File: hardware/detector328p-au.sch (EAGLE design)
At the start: 65 parts, among them K1 SRD-05VDC-SL-C, Q1 BSS123, Q2 16MHz, T1 BC817-40SMD, T2 BC817, T3 BC817, U1 ATMEGA328P-AU

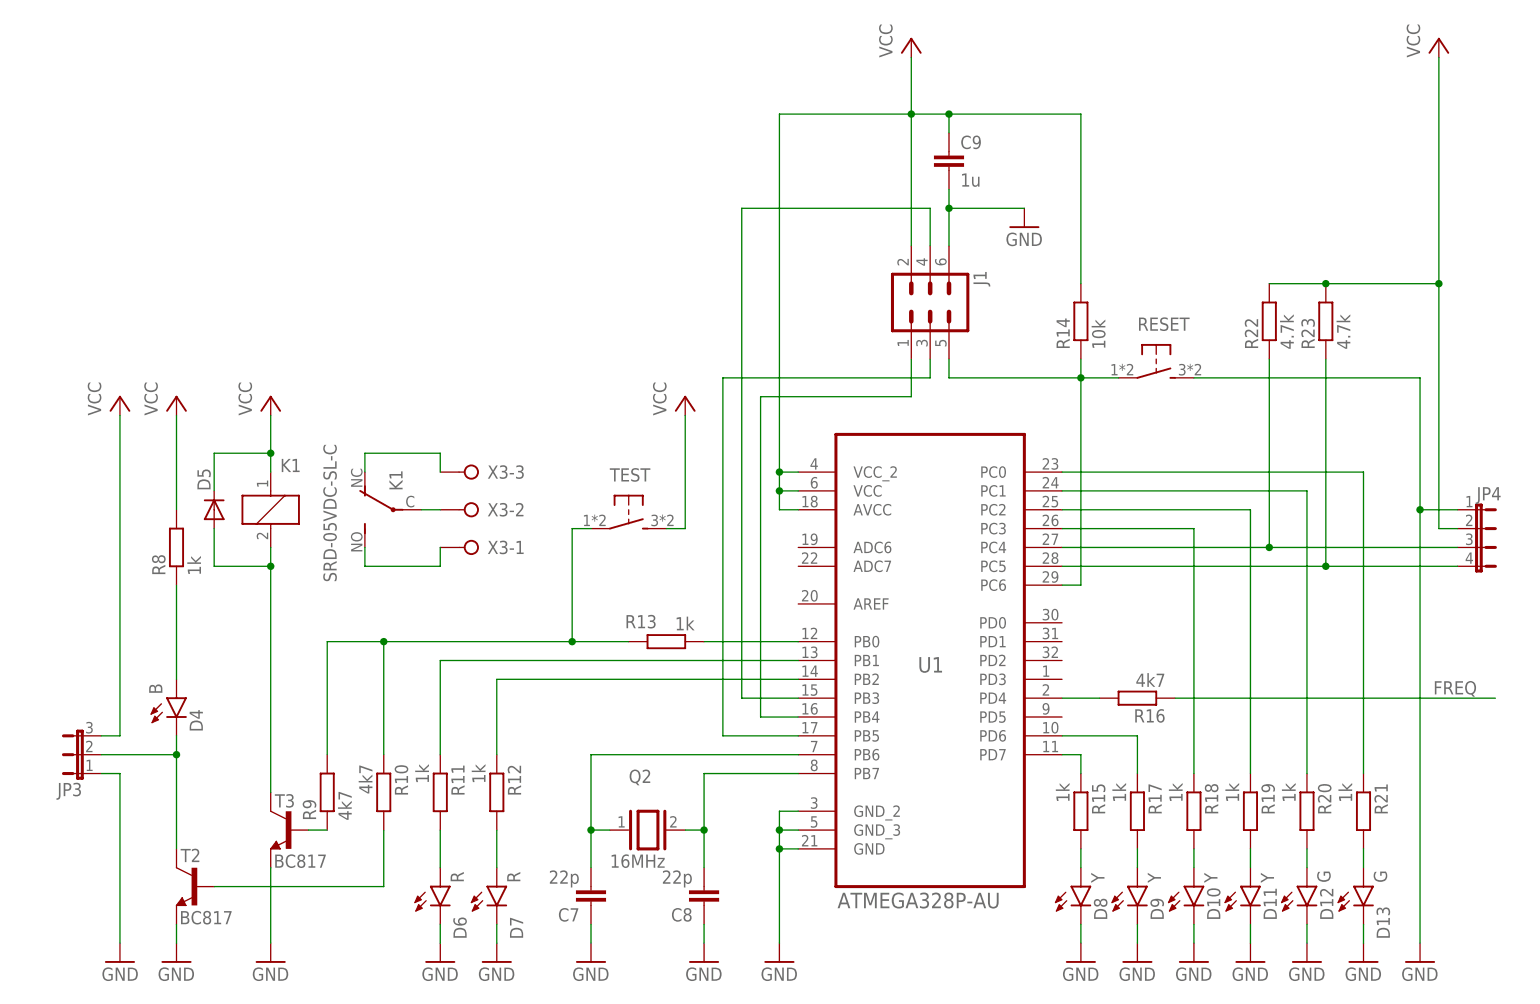
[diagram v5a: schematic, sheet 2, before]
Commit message: detector328p-au almost wired
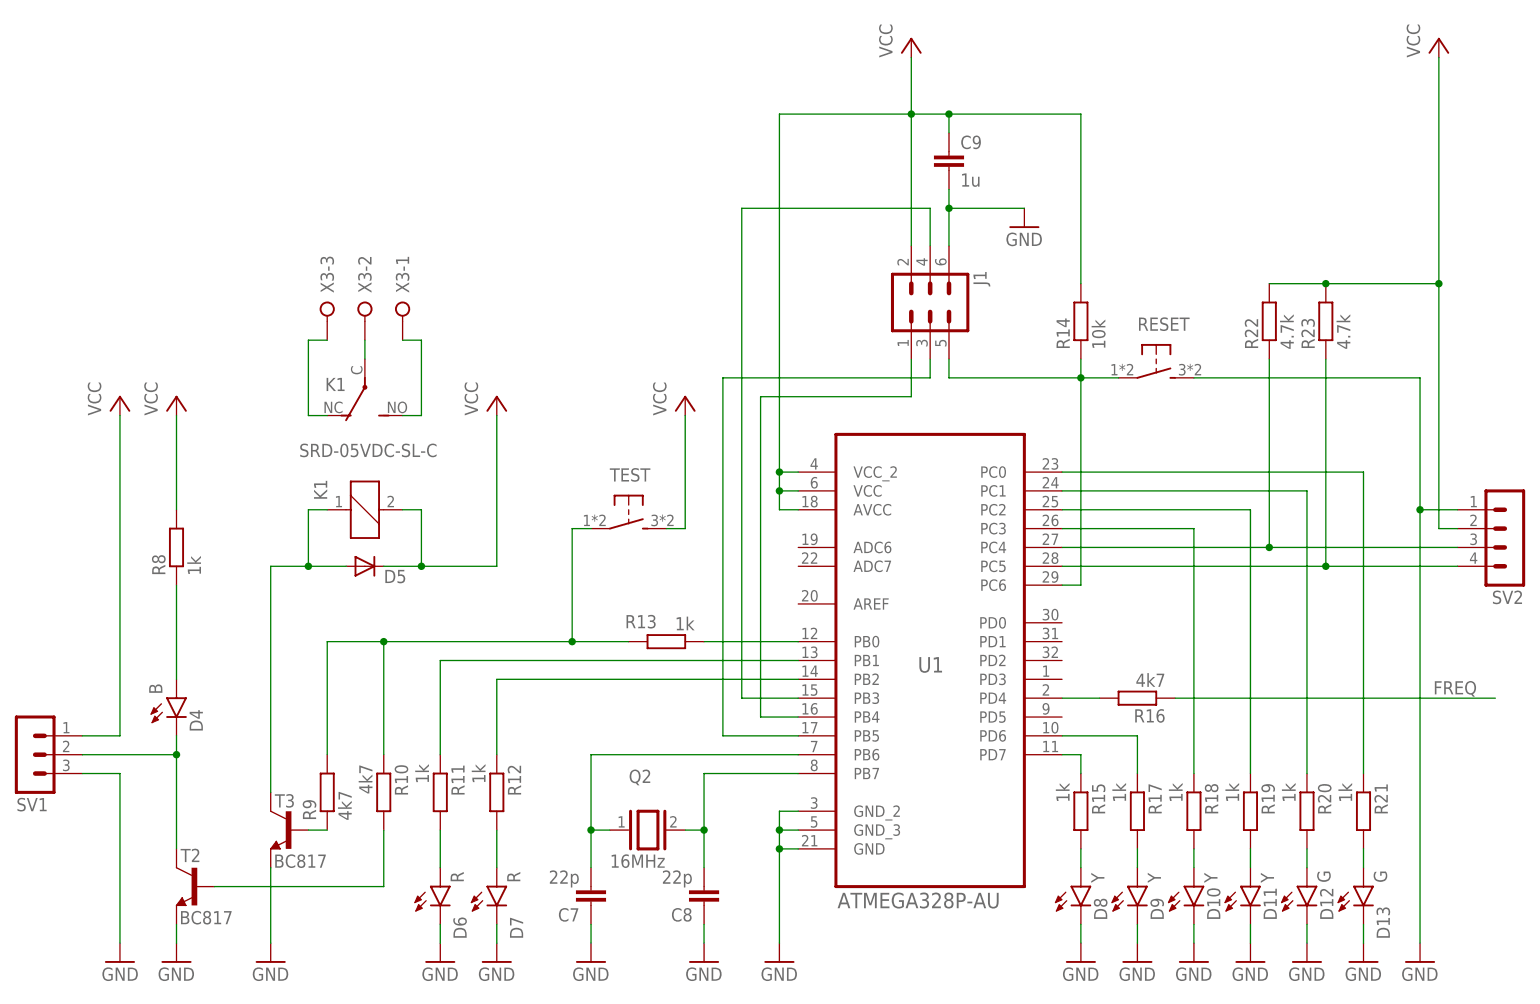
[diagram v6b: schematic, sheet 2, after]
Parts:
- removed JP2: (no value), jumper:JP3QE
- removed JP3: (no value), jumper:JP2E
- removed JP4: (no value), jumper:JP4E
- added SV1: (no value), con-lstb:MA03-1
- added SV2: (no value), con-lstb:MA04-1
- added SV3: (no value), con-lstb:MA03-2
- JP1: device jumper:JP3QE -> detector:JP3QE
- X1, X3: device con-wago-508:W237-03P -> detector:W237-3E
- X2: device con-wago-500:W237-102 -> detector:W237-02P
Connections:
- removed net N$39: D5.A, K11.2, T3.C
- new net N$38: D5.A, K11.1, T3.C
- net GND: now also SV1.3, SV2.1, SV3.2, SV3.4, SV3.6; no longer JP2-1.2, JP2-2.2, JP2-3.2, JP3.1, JP4.1
- net N$23: now also SV1.2; no longer JP3.2
- net N$44: now also SV2.4; no longer JP4.4
- net N$45: now also SV2.3; no longer JP4.3
- net VCC: now also K11.2, SV1.1, SV2.2, SV3.1, SV3.3, SV3.5; no longer JP2-1.1, JP2-2.1, JP2-3.1, JP3.3, JP4.2, K11.1
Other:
- moved on the sheet: C6, D5, K1, X3-1, X3-2, X3-3

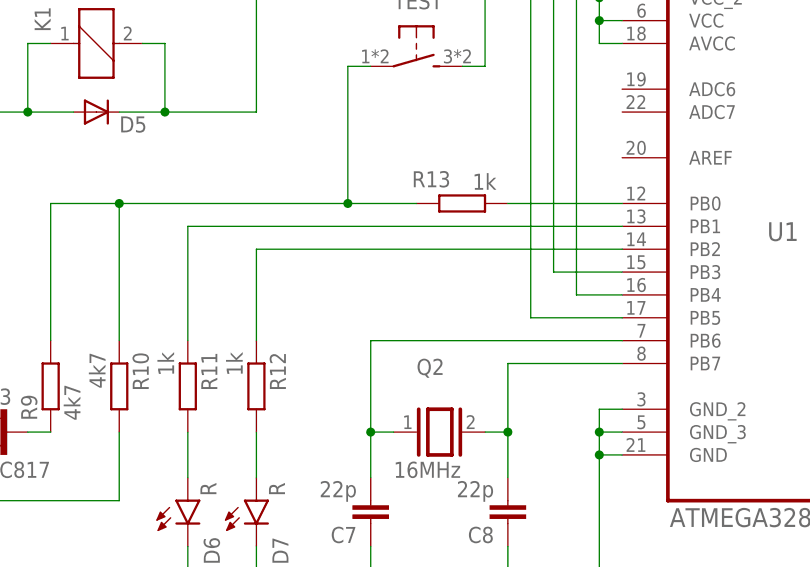
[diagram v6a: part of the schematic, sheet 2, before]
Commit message: detector328p-au wiring ready, labels need fixing
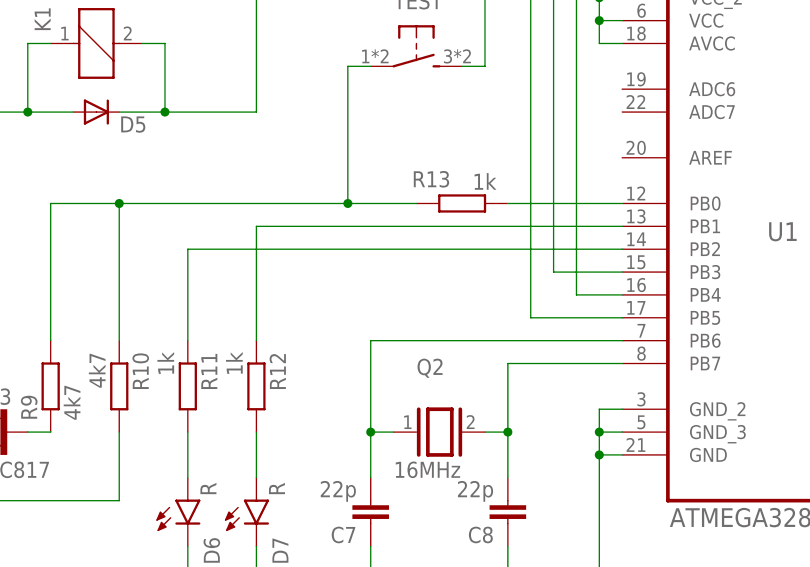
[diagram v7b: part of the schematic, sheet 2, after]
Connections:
- net N$36: now also R11.1; no longer R12.1
- net N$37: now also R12.1; no longer R11.1
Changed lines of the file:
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@@
 <net name="N$36" class="0">
 <segment>
-<pinref part="R12" gate="G$1" pin="1"/>
 <pinref part="U1" gate="A" pin="PB2"/>
-<wire x1="60.96" y1="38.1" x2="60.96" y2="48.26" width="0.1524" layer="91"/>
-<wire x1="60.96" y1="48.26" x2="101.6" y2="48.26" width="0.1524" layer="91"/>
+<wire x1="53.34" y1="48.26" x2="101.6" y2="48.26" width="0.1524" layer="91"/>
+<pinref part="R11" gate="G$1" pin="1"/>
+<wire x1="53.34" y1="48.26" x2="53.34" y2="38.1" width="0.1524" layer="91"/>
 </segment>
 </net>
 <net name="N$37" class="0">
 <segment>
-<pinref part="R11" gate="G$1" pin="1"/>
 <pinref part="U1" gate="A" pin="PB1"/>
-<wire x1="53.34" y1="38.1" x2="53.34" y2="50.8" width="0.1524" layer="91"/>
-<wire x1="53.34" y1="50.8" x2="101.6" y2="50.8" width="0.1524" layer="91"/>
+<wire x1="60.96" y1="50.8" x2="101.6" y2="50.8" width="0.1524" layer="91"/>
+<pinref part="R12" gate="G$1" pin="1"/>
+<wire x1="60.96" y1="50.8" x2="60.96" y2="38.1" width="0.1524" layer="91"/>
 </segment>
 </net>

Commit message: detector328p-au final
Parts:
- renumbered SV1 to OUT, SV2 to LCD, SV3 to POWER
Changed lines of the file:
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@@
 <part name="TEST" library="detector" deviceset="10-XX" device=""/>
 <part name="RESET" library="detector" deviceset="10-XX" device=""/>
-<part name="SV1" library="con-lstb" deviceset="MA03-1" device=""/>
-<part name="SV2" library="con-lstb" deviceset="MA04-1" device=""/>
-<part name="SV3" library="con-lstb" deviceset="MA03-2" device=""/>
+<part name="OUT" library="con-lstb" deviceset="MA03-1" device=""/>
+<part name="LCD" library="con-lstb" deviceset="MA04-1" device=""/>
+<part name="POWER" library="con-lstb" deviceset="MA03-2" device=""/>
 </parts>
 <sheets>
@@
 <attribute name="VALUE" x="109.982" y="54.61" size="1.778" layer="96" rot="R90"/>
 </instance>
-<instance part="SV3" gate="1" x="165.1" y="40.64" rot="MR0"/>
+<instance part="POWER" gate="1" x="165.1" y="40.64" rot="MR0"/>
 </instances>
 <busses>
@@
 <wire x1="177.8" y1="15.24" x2="172.72" y2="15.24" width="0.1524" layer="91"/>
 <junction x="172.72" y="15.24"/>
-<pinref part="SV3" gate="1" pin="2"/>
+<pinref part="POWER" gate="1" pin="2"/>
 <junction x="172.72" y="38.1"/>
-<pinref part="SV3" gate="1" pin="4"/>
+<pinref part="POWER" gate="1" pin="4"/>
 <junction x="172.72" y="40.64"/>
-<pinref part="SV3" gate="1" pin="6"/>
+<pinref part="POWER" gate="1" pin="6"/>
 <junction x="172.72" y="43.18"/>
 </segment>
@@
 <wire x1="177.8" y1="25.4" x2="177.8" y2="33.02" width="0.1524" layer="91"/>
 <junction x="177.8" y="33.02"/>
-<pinref part="SV3" gate="1" pin="1"/>
+<pinref part="POWER" gate="1" pin="1"/>
 <junction x="157.48" y="38.1"/>
-<pinref part="SV3" gate="1" pin="3"/>
+<pinref part="POWER" gate="1" pin="3"/>
 <junction x="157.48" y="40.64"/>
-<pinref part="SV3" gate="1" pin="5"/>
+<pinref part="POWER" gate="1" pin="5"/>
 <junction x="157.48" y="43.18"/>
 </segment>
@@
 <instance part="TEST" gate="1" x="78.74" y="68.58" rot="R270"/>
 <instance part="RESET" gate="1" x="149.86" y="88.9" rot="R270"/>
-<instance part="SV1" gate="G$1" x="-2.54" y="38.1" rot="MR180"/>
-<instance part="SV2" gate="1" x="198.12" y="66.04" rot="R180"/>
+<instance part="OUT" gate="G$1" x="-2.54" y="38.1" rot="MR180"/>
+<instance part="LCD" gate="1" x="198.12" y="66.04" rot="R180"/>
 </instances>
 <busses>
@@
 <pinref part="GND10" gate="1" pin="GND"/>
 <wire x1="10.16" y1="12.7" x2="10.16" y2="35.56" width="0.1524" layer="91"/>
-<pinref part="SV1" gate="G$1" pin="3"/>
+<pinref part="OUT" gate="G$1" pin="3"/>
 <wire x1="10.16" y1="35.56" x2="5.08" y2="35.56" width="0.1524" layer="91"/>
 </segment>
@@
 <junction x="185.42" y="71.12"/>
 <pinref part="RESET" gate="1" pin="S"/>
-<pinref part="SV2" gate="1" pin="1"/>
+<pinref part="LCD" gate="1" pin="1"/>
 </segment>
 </net>
@@
 <pinref part="P+4" gate="VCC" pin="VCC"/>
 <wire x1="10.16" y1="40.64" x2="10.16" y2="83.82" width="0.1524" layer="91"/>
-<pinref part="SV1" gate="G$1" pin="1"/>
+<pinref part="OUT" gate="G$1" pin="1"/>
 <wire x1="10.16" y1="40.64" x2="5.08" y2="40.64" width="0.1524" layer="91"/>
 </segment>
@@
 <junction x="172.72" y="101.6"/>
 <junction x="187.96" y="101.6"/>
-<pinref part="SV2" gate="1" pin="2"/>
+<pinref part="LCD" gate="1" pin="2"/>
 </segment>
 <segment>
@@
 <wire x1="17.78" y1="38.1" x2="17.78" y2="25.4" width="0.1524" layer="91"/>
 <pinref part="T2" gate="G$1" pin="C"/>
-<pinref part="SV1" gate="G$1" pin="2"/>
+<pinref part="OUT" gate="G$1" pin="2"/>
 <wire x1="5.08" y1="38.1" x2="17.78" y2="38.1" width="0.1524" layer="91"/>
 <junction x="17.78" y="38.1"/>
@@
 <wire x1="172.72" y1="91.44" x2="172.72" y2="63.5" width="0.1524" layer="91"/>
 <junction x="172.72" y="63.5"/>
-<pinref part="SV2" gate="1" pin="4"/>
+<pinref part="LCD" gate="1" pin="4"/>
 </segment>
 </net>
@@
 <wire x1="165.1" y1="66.04" x2="165.1" y2="91.44" width="0.1524" layer="91"/>
 <junction x="165.1" y="66.04"/>
-<pinref part="SV2" gate="1" pin="3"/>
-</segment>
-</net>
+<pinref part="LCD" gate="1" pin="3"/>
+</segment>
+</net>
